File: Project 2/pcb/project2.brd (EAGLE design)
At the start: 160 x 100 mm, 5 parts, among them SW1 PUSH_BUTTON, U1 POCKETBEAGLE

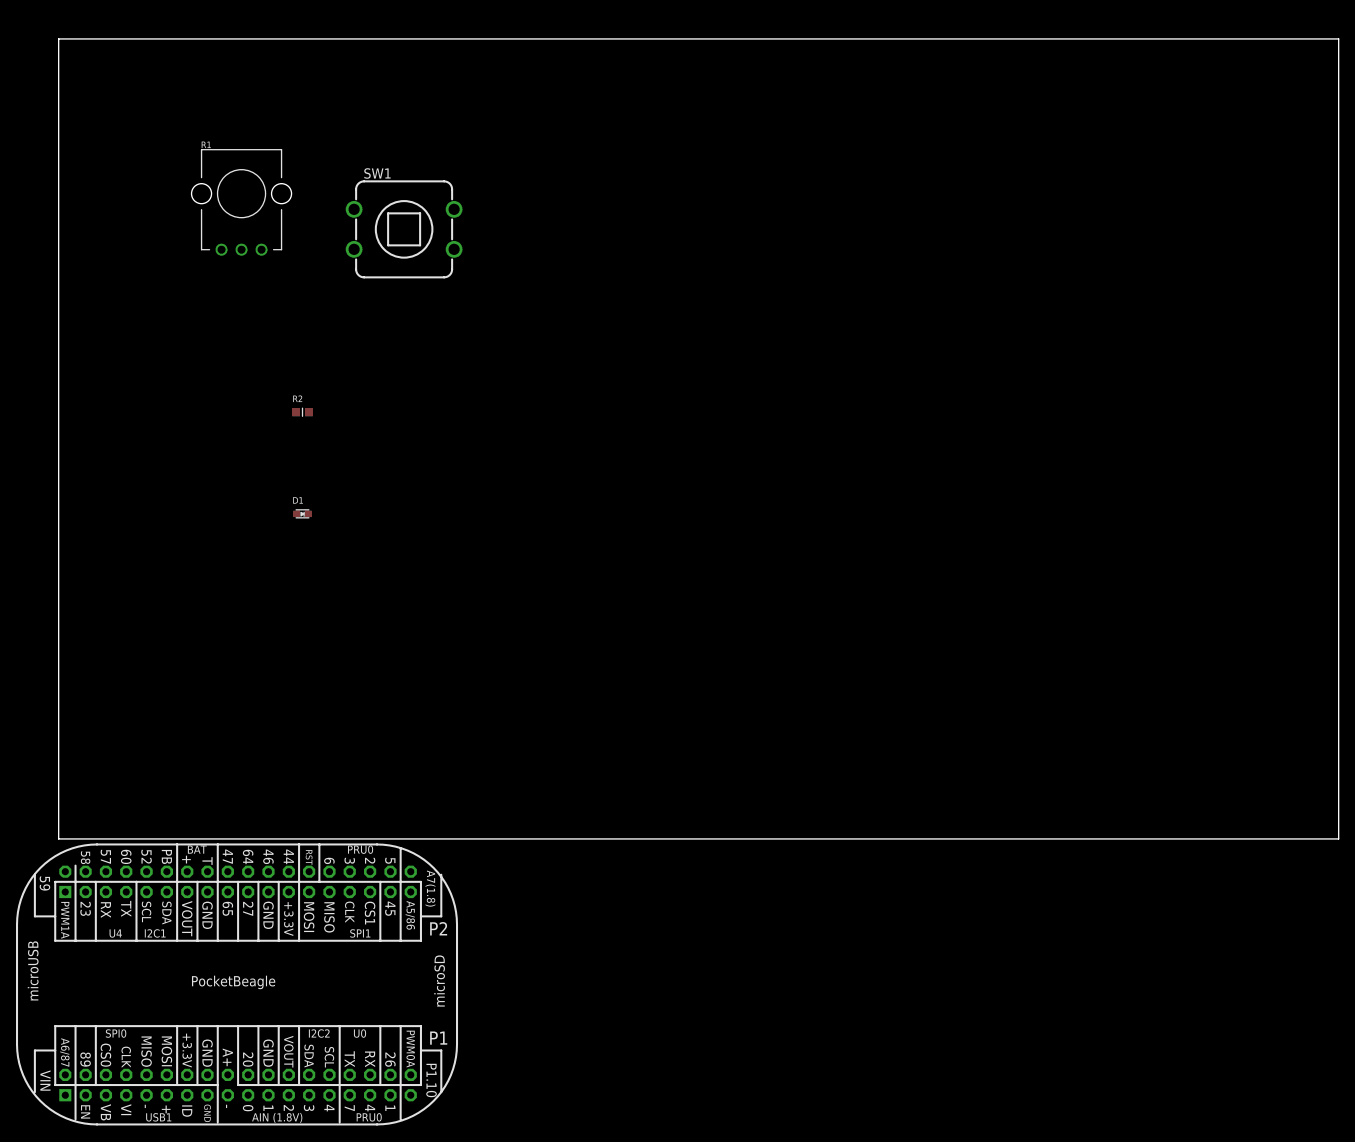
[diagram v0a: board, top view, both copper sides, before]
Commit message: Sunday night update
SPI board throwing errors, MacroFab website cannot process .brd as a result.
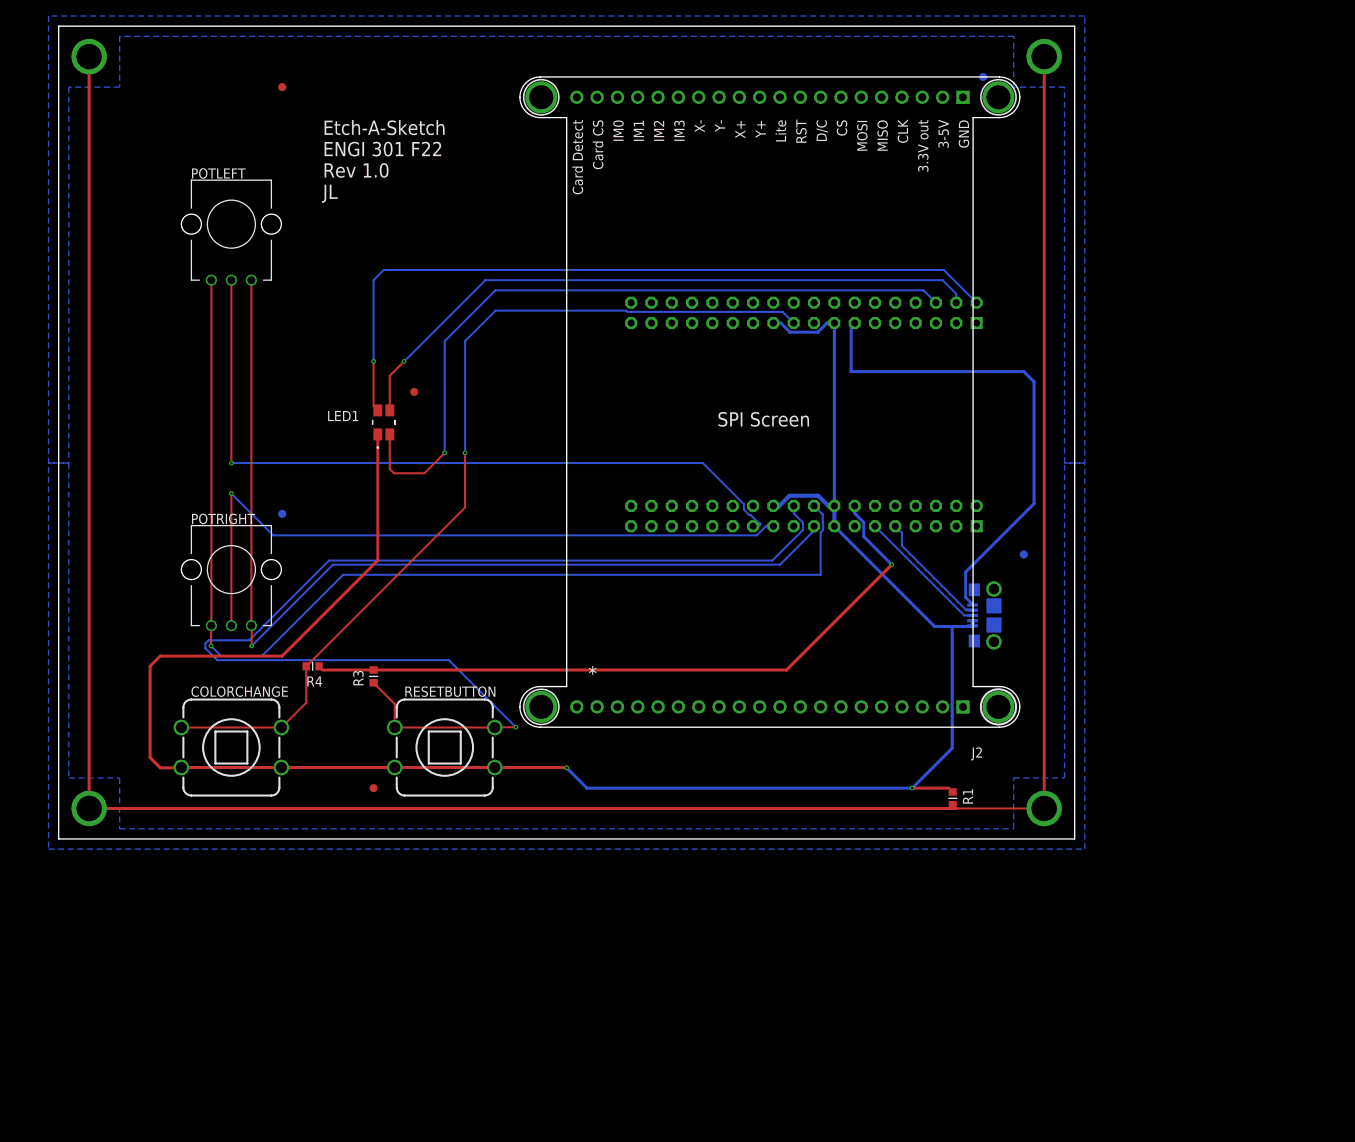
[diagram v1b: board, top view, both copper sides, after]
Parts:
- removed D1: LED, project2lib:EIA-STD
- removed R2: (no value), project2lib:R0603
- removed SW1: PUSH_BUTTON, project2lib:BUTTON_12.5MM
- added COLORCHANGE, RESETBUTTON: PUSH_BUTTON, project2lib:BUTTON_12.5MM
- added FUD1, FUD2, FUD3, FUD4, FUD5, FUD6: FIDUCIAL, project2:FIDUCIAL_40MIL
- added J1: 10118193-0001LF, 10118193-0001LF:101181930001LF
- added J2: SPI_LCD, project2:TFT_LCD_PCB
- added LED1: ASMB-MTB0-0A3A2, project2lib:ASMBMTB00A3A2
- added MGT1, MGT2, MGT3, MGT4: MOUNTING_HOLE, project2:MOUNTING_HOLE
- added POTLEFT, POTRIGHT: POTENTIOMETER, project2lib:POT-PO90S
- added R3, R4: 1K, project2lib:R0603
- R1: value POTENTIOMETER -> 0.1K; device project2lib:POT-PO90S -> project2:R0603
- moved U1 144.5 mm to (120.7, 35.6), flipped to the bottom
- moved R1 112.3 mm to (111.8, 5.08), turned to 270 degrees
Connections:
- new net CGND: MGT1.P$1, MGT2.P$1, MGT3.P$1, MGT4.P$1, R1.2
- new net N$1: POTRIGHT.S, U1.P1_21
- new net N$10: J2.9@JP2, U1.P1_02
- new net N$12: COLORCHANGE.1, COLORCHANGE.3, R4.2, U1.P2_19
- new net N$13: LED1.2, U1.P2_02
- new net N$14: LED1.3, U1.P2_04
- new net N$15: LED1.4, U1.P2_06
- new net N$17: J1.2, U1.P1_09
- new net N$18: J1.3, U1.P1_11
- new net N$2: POTLEFT.S, U1.P1_23
- new net N$3: POTLEFT.CW, POTRIGHT.CW, U1.P1_17
- new net N$4: R3.1, RESETBUTTON.1, RESETBUTTON.3, U1.P1_20
- new net N$5: J2.4@JP2, U1.P1_08
- new net N$6: J2.5@JP2, U1.P1_10
- new net N$7: J2.6@JP2, U1.P1_12
- new net N$8: J2.7@JP2, U1.P1_06
- new net N$9: J2.8@JP2, U1.P1_04
- new net VDD_1P8V: POTLEFT.CCW, POTRIGHT.CCW, U1.P1_18
- new net VDD_3P3V: J2.3@JP2, R3.2, R4.1, U1.P1_14
- new net VDD_5V: J1.1, U1.P2_13
- net 3.3V: no longer U1.P1_14
- net GND: now also COLORCHANGE.2, COLORCHANGE.4, J1.4, J1.5, J2.1@JP2, LED1.1, R1.1, RESETBUTTON.2, RESETBUTTON.4, U1.P1_15
- net VOUT: no longer U1.P2_13
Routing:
- net CGND: track 0.00 -> 308.0 mm
- net GND: track 0.00 -> 252.1 mm, vias 0 -> 2
- net N$4: track 0.00 -> 149.4 mm, vias 0 -> 1
- net VDD_1P8V: track 0.00 -> 135.9 mm, vias 0 -> 1
- net N$3: track 0.00 -> 122.5 mm, vias 0 -> 1
- net N$12: track 0.00 -> 113.6 mm, vias 0 -> 1
- net N$13: track 0.00 -> 94.1 mm, vias 0 -> 1
- net N$2: track 0.00 -> 93.4 mm, vias 0 -> 1
- net N$15: track 0.00 -> 91.1 mm, vias 0 -> 1
- net N$1: track 0.00 -> 86.9 mm, vias 0 -> 1
- net VDD_3P3V: track 0.00 -> 86.5 mm, vias 0 -> 1
- net N$14: track 0.00 -> 81.9 mm, vias 0 -> 1
- net VDD_5V: track 0.00 -> 61.4 mm
- net N$18: track 0.00 -> 16.8 mm
- net N$17: track 0.00 -> 14.9 mm
- added copper zone on layer 16, net CGND
- added copper zone on layer 2, net GND
- added copper zone on layer 15, net VDD_3P3V
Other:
- board size 160 x 100 mm -> 127 x 101.6 mm
- board text added: "Etch-A-Sketch ENGI 301 F22 Rev 1.0 JL"
